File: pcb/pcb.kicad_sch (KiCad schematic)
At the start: 65 parts, among them J1 RJ45, J2 RJ45, SW1 Keyswitch, SW10 Keyswitch, SW11 Keyswitch, SW12 Keyswitch, SW13 Keyswitch, SW14 Keyswitch, SW15 Keyswitch, SW16 Keyswitch, SW17 Keyswitch, SW18 Keyswitch, SW19 Keyswitch, SW2 Keyswitch, SW20 Keyswitch, SW21 Keyswitch, SW22 Keyswitch, SW23 Keyswitch, SW24 Keyswitch, SW25 Keyswitch, SW26 Keyswitch, SW27 Keyswitch, SW28 Keyswitch, SW29 Keyswitch, SW3 Keyswitch, SW30 Keyswitch, SW4 Keyswitch, SW5 Keyswitch, SW6 Keyswitch, SW7 Keyswitch, SW8 Keyswitch, SW9 Keyswitch

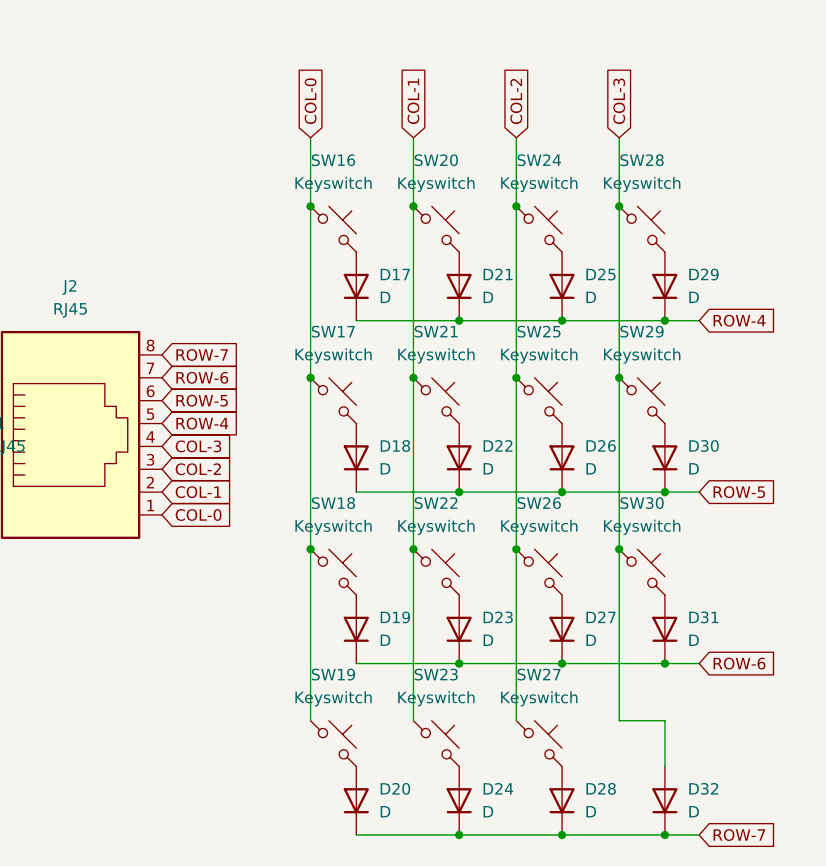
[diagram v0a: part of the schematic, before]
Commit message: add pcb right hand layout
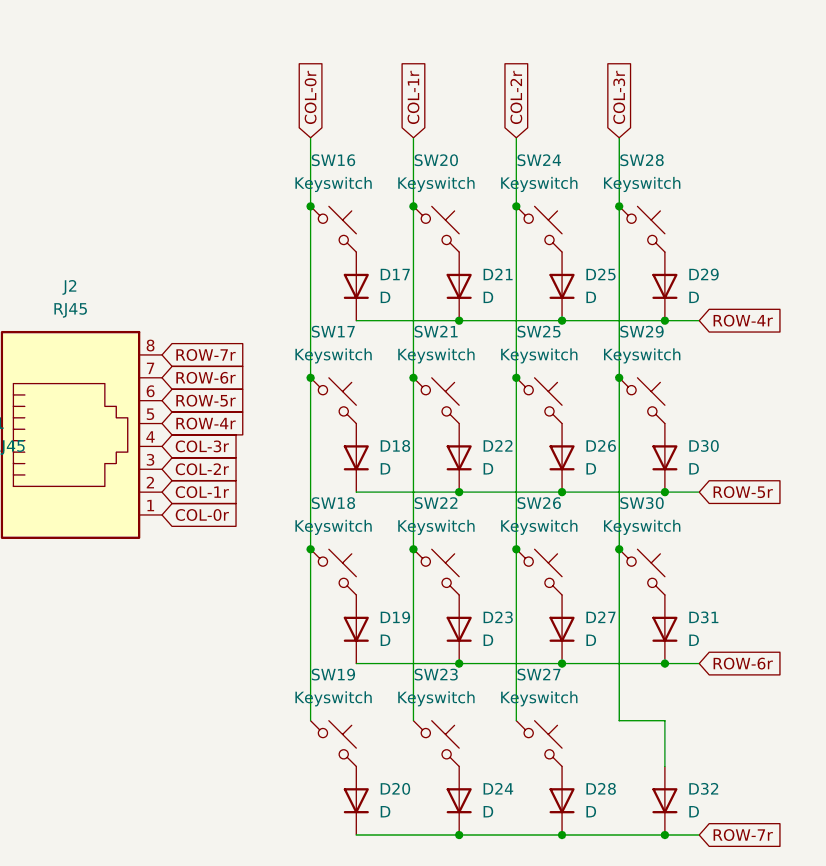
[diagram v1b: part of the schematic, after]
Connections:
- net COL-0: no longer J2.1, SW16.1, SW17.1, SW18.1, SW19.1
- net COL-1: no longer J2.2, SW20.1, SW21.1, SW22.1, SW23.1
- net COL-2: no longer J2.3, SW24.1, SW25.1, SW26.1, SW27.1
- net COL-3: no longer D32.2 (A), J2.4, SW28.1, SW29.1, SW30.1
- net ROW-4: no longer D17.1 (K), D21.1 (K), D25.1 (K), D29.1 (K), J2.5
- net ROW-5: no longer D18.1 (K), D22.1 (K), D26.1 (K), D30.1 (K), J2.6
- net ROW-6: no longer D19.1 (K), D23.1 (K), D27.1 (K), D31.1 (K), J2.7
- net ROW-7: no longer D20.1 (K), D24.1 (K), D28.1 (K), D32.1 (K), J2.8
- new net COL-0r: J2.1, SW16.1, SW17.1, SW18.1, SW19.1
- new net COL-1r: J2.2, SW20.1, SW21.1, SW22.1, SW23.1
- new net COL-2r: J2.3, SW24.1, SW25.1, SW26.1, SW27.1
- new net COL-3r: D32.2 (A), J2.4, SW28.1, SW29.1, SW30.1
- new net ROW-4r: D17.1 (K), D21.1 (K), D25.1 (K), D29.1 (K), J2.5
- new net ROW-5r: D18.1 (K), D22.1 (K), D26.1 (K), D30.1 (K), J2.6
- new net ROW-6r: D19.1 (K), D23.1 (K), D27.1 (K), D31.1 (K), J2.7
- new net ROW-7r: D20.1 (K), D24.1 (K), D28.1 (K), D32.1 (K), J2.8

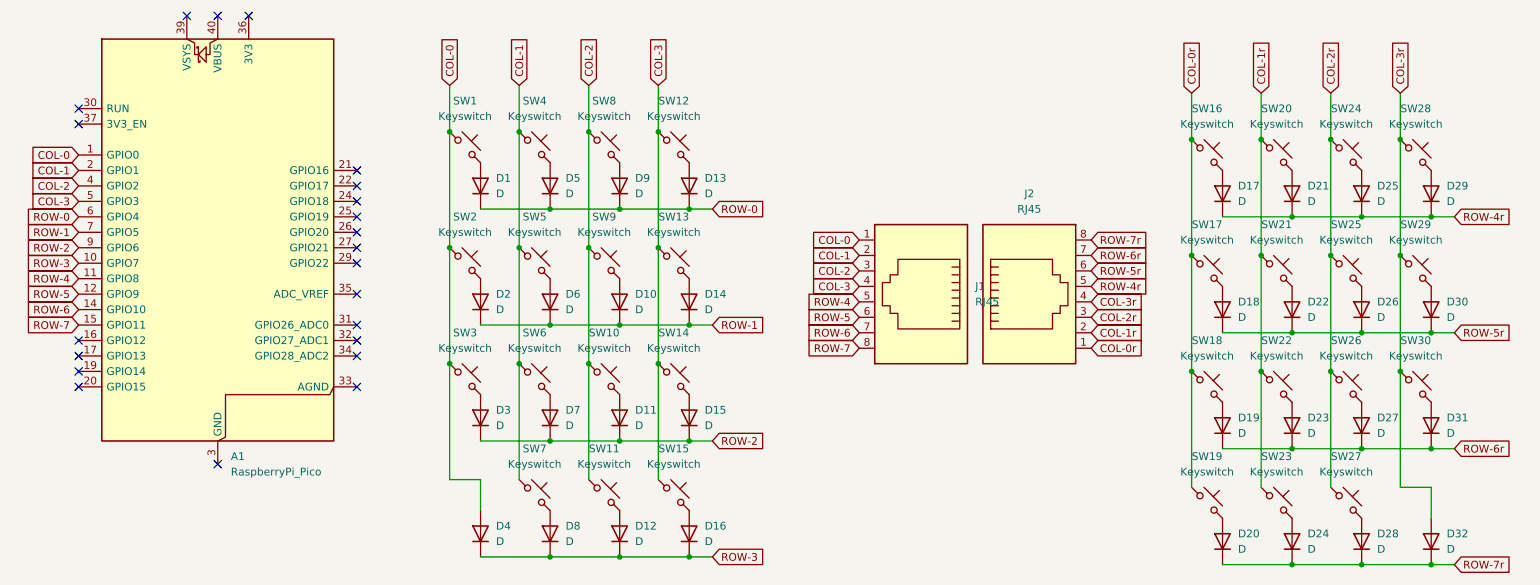
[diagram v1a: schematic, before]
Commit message: add pcb screw holes
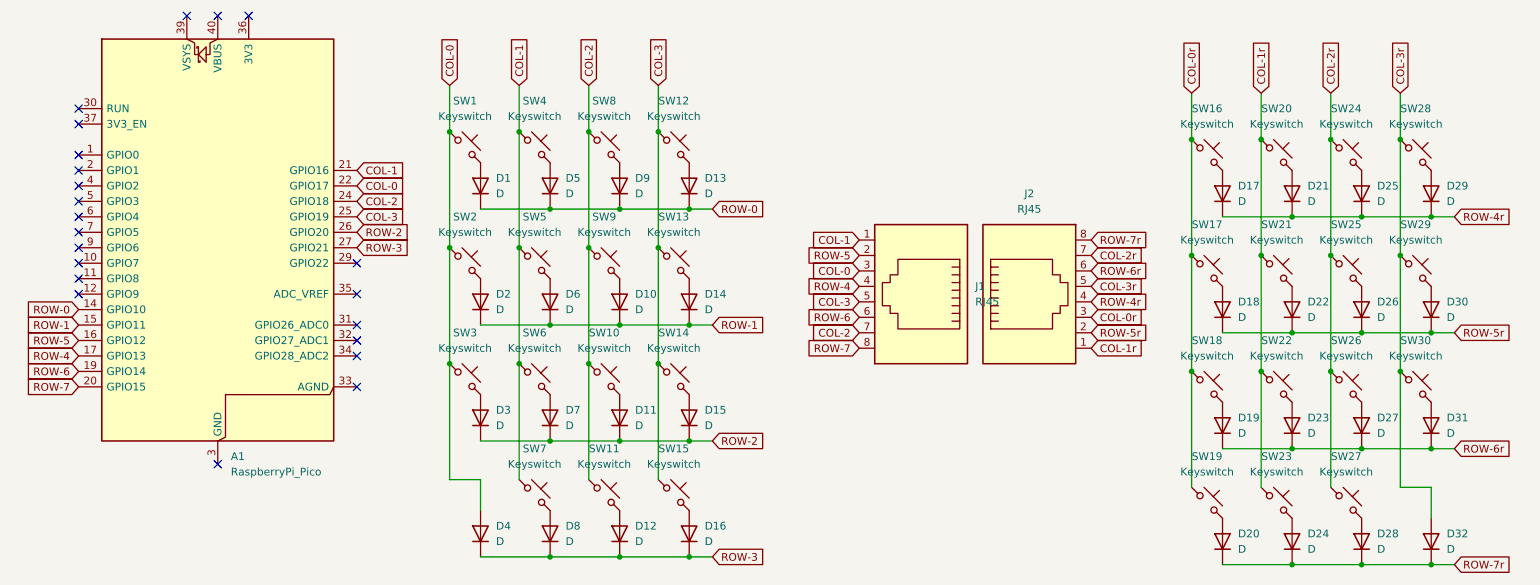
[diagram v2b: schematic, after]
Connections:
- net COL-0: now also A1.22 (GPIO17), J1.3; no longer A1.1 (GPIO0), J1.1
- net COL-0r: now also J2.3; no longer J2.1
- net COL-1: now also A1.21 (GPIO16), J1.1; no longer A1.2 (GPIO1), J1.2
- net COL-1r: now also J2.1; no longer J2.2
- net COL-2: now also A1.24 (GPIO18), J1.7; no longer A1.4 (GPIO2), J1.3
- net COL-2r: now also J2.7; no longer J2.3
- net COL-3: now also A1.25 (GPIO19), J1.5; no longer A1.5 (GPIO3), J1.4
- net COL-3r: now also J2.5; no longer J2.4
- net ROW-0: now also A1.14 (GPIO10); no longer A1.6 (GPIO4)
- net ROW-1: now also A1.15 (GPIO11); no longer A1.7 (GPIO5)
- net ROW-2: now also A1.26 (GPIO20); no longer A1.9 (GPIO6)
- net ROW-3: now also A1.27 (GPIO21); no longer A1.10 (GPIO7)
- net ROW-4: now also A1.17 (GPIO13), J1.4; no longer A1.11 (GPIO8), J1.5
- net ROW-4r: now also J2.4; no longer J2.5
- net ROW-5: now also A1.16 (GPIO12), J1.2; no longer A1.12 (GPIO9), J1.6
- net ROW-5r: now also J2.2; no longer J2.6
- net ROW-6: now also A1.19 (GPIO14), J1.6; no longer A1.14 (GPIO10), J1.7
- net ROW-6r: now also J2.6; no longer J2.7
- net ROW-7: now also A1.20 (GPIO15); no longer A1.15 (GPIO11)

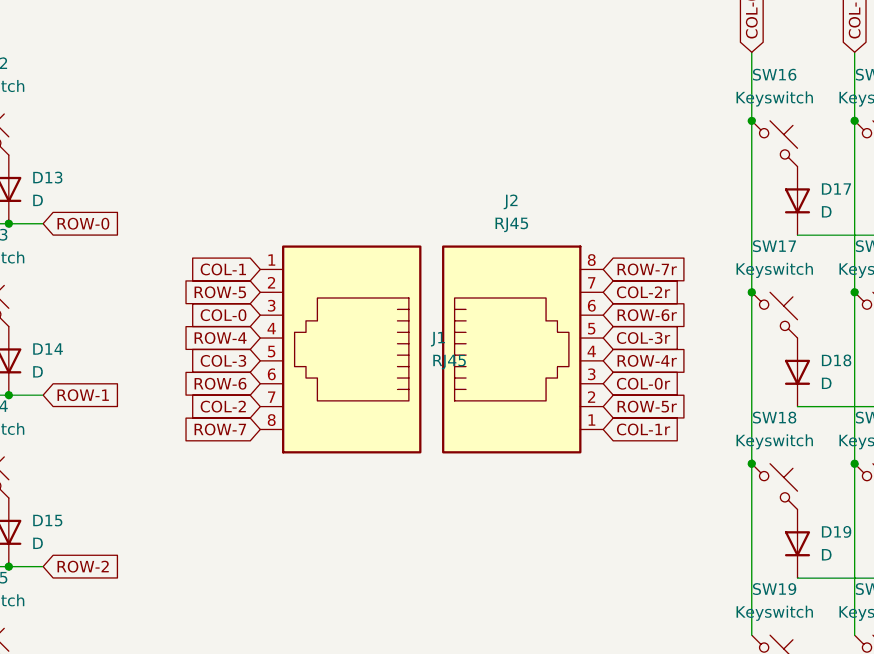
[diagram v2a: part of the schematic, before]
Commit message: fix pcb holes
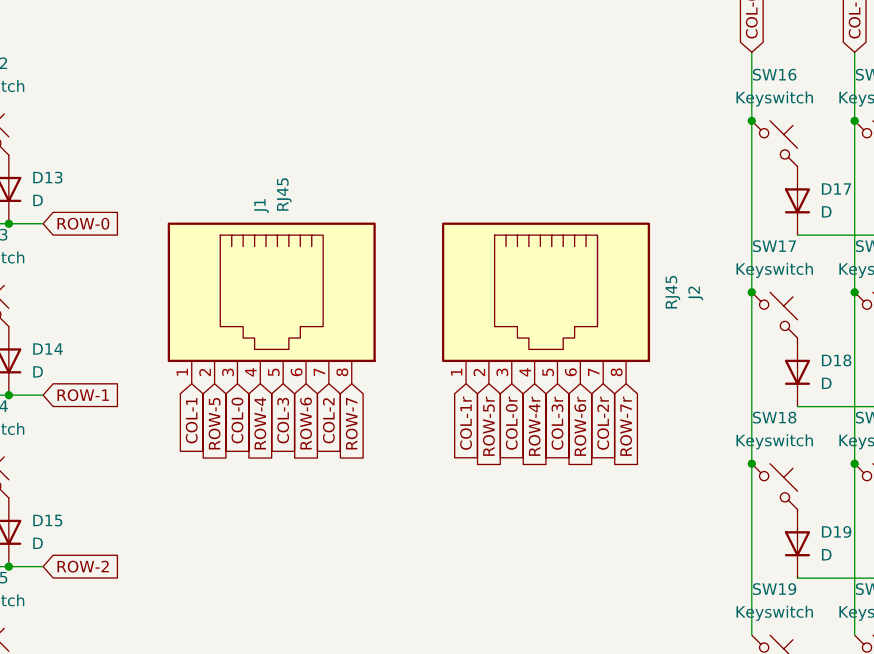
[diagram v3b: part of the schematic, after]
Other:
- moved on the sheet: J1, J2
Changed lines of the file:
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@@
 	(global_label "COL-1r"
 		(shape input)
-		(at 194.31 73.66 0)
+		(at 179.07 68.58 270)
 		(fields_autoplaced yes)
 		(effects
@@
 				(size 1.27 1.27)
 			)
-			(justify left)
+			(justify right)
 		)
 		(property "Intersheetrefs" "${INTERSHEET_REFS}"
-			(at 204.4919 73.66 0)
+			(at 179.07 78.7619 90)
 			(effects
 				(font
 					(size 1.27 1.27)
 				)
-				(justify left)
+				(justify right)
 				(hide yes)
 			)
@@
 	(global_label "ROW-6r"
 		(shape input)
-		(at 194.31 60.96 0)
+		(at 191.77 68.58 270)
 		(fields_autoplaced yes)
 		(effects
@@
 				(size 1.27 1.27)
 			)
-			(justify left)
+			(justify right)
 		)
 		(property "Intersheetrefs" "${INTERSHEET_REFS}"
-			(at 204.9152 60.96 0)
+			(at 191.77 79.1852 90)
 			(effects
 				(font
 					(size 1.27 1.27)
 				)
-				(justify left)
+				(justify right)
 				(hide yes)
 			)
@@
 	(global_label "ROW-5"
 		(shape input)
-		(at 156.21 58.42 180)
+		(at 151.13 68.58 270)
 		(fields_autoplaced yes)
 		(effects
@@
 		)
 		(property "Intersheetrefs" "${INTERSHEET_REFS}"
-			(at 146.391 58.42 0)
+			(at 151.13 78.399 90)
 			(effects
 				(font
@@
 	(global_label "ROW-4"
 		(shape input)
-		(at 156.21 63.5 180)
+		(at 156.21 68.58 270)
 		(fields_autoplaced yes)
 		(effects
@@
 		)
 		(property "Intersheetrefs" "${INTERSHEET_REFS}"
-			(at 146.391 63.5 0)
+			(at 156.21 78.399 90)
 			(effects
 				(font
@@
 	(global_label "ROW-4r"
 		(shape input)
-		(at 194.31 66.04 0)
+		(at 186.69 68.58 270)
 		(fields_autoplaced yes)
 		(effects
@@
 				(size 1.27 1.27)
 			)
-			(justify left)
+			(justify right)
 		)
 		(property "Intersheetrefs" "${INTERSHEET_REFS}"
-			(at 204.9152 66.04 0)
+			(at 186.69 79.1852 90)
 			(effects
 				(font
 					(size 1.27 1.27)
 				)
-				(justify left)
+				(justify right)
 				(hide yes)
 			)
@@
 	(global_label "ROW-7"
 		(shape input)
-		(at 156.21 73.66 180)
+		(at 166.37 68.58 270)
 		(fields_autoplaced yes)
 		(effects
@@
 		)
 		(property "Intersheetrefs" "${INTERSHEET_REFS}"
-			(at 146.391 73.66 0)
+			(at 166.37 78.399 90)
 			(effects
 				(font
@@
 	(global_label "COL-2"
 		(shape input)
-		(at 156.21 71.12 180)
+		(at 163.83 68.58 270)
 		(fields_autoplaced yes)
 		(effects
@@
 		)
 		(property "Intersheetrefs" "${INTERSHEET_REFS}"
-			(at 146.8143 71.12 0)
+			(at 163.83 77.9757 90)
 			(effects
 				(font
@@
 	(global_label "ROW-5r"
 		(shape input)
-		(at 194.31 71.12 0)
+		(at 181.61 68.58 270)
 		(fields_autoplaced yes)
 		(effects
@@
 				(size 1.27 1.27)
 			)
-			(justify left)
+			(justify right)
 		)
 		(property "Intersheetrefs" "${INTERSHEET_REFS}"
-			(at 204.9152 71.12 0)
+			(at 181.61 79.1852 90)
 			(effects
 				(font
 					(size 1.27 1.27)
 				)
-				(justify left)
+				(justify right)
 				(hide yes)
 			)
@@
 	(global_label "ROW-6"
 		(shape input)
-		(at 156.21 68.58 180)
+		(at 161.29 68.58 270)
 		(fields_autoplaced yes)
 		(effects
@@
 		)
 		(property "Intersheetrefs" "${INTERSHEET_REFS}"
-			(at 146.391 68.58 0)
+			(at 161.29 78.399 90)
 			(effects
 				(font
@@
 	(global_label "ROW-7r"
 		(shape input)
-		(at 194.31 55.88 0)
+		(at 196.85 68.58 270)
 		(fields_autoplaced yes)
 		(effects
@@
 				(size 1.27 1.27)
 			)
-			(justify left)
+			(justify right)
 		)
 		(property "Intersheetrefs" "${INTERSHEET_REFS}"
-			(at 204.9152 55.88 0)
+			(at 196.85 79.1852 90)
 			(effects
 				(font
 					(size 1.27 1.27)
 				)
-				(justify left)
+				(justify right)
 				(hide yes)
 			)
@@
 	(global_label "COL-3r"
 		(shape input)
-		(at 194.31 63.5 0)
+		(at 189.23 68.58 270)
 		(fields_autoplaced yes)
 		(effects
@@
 				(size 1.27 1.27)
 			)
-			(justify left)
+			(justify right)
 		)
 		(property "Intersheetrefs" "${INTERSHEET_REFS}"
-			(at 204.4919 63.5 0)
+			(at 189.23 78.7619 90)
 			(effects
 				(font
 					(size 1.27 1.27)
 				)
-				(justify left)
+				(justify right)
 				(hide yes)
 			)
@@
 	(global_label "COL-0r"
 		(shape input)
-		(at 194.31 68.58 0)
+		(at 184.15 68.58 270)
 		(fields_autoplaced yes)
 		(effects
@@
 				(size 1.27 1.27)
 			)
-			(justify left)
+			(justify right)
 		)
 		(property "Intersheetrefs" "${INTERSHEET_REFS}"
-			(at 204.4919 68.58 0)
+			(at 184.15 78.7619 90)
 			(effects
 				(font
 					(size 1.27 1.27)
 				)
-				(justify left)
+				(justify right)
 				(hide yes)
 			)
@@
 	(global_label "COL-2r"
 		(shape input)
-		(at 194.31 58.42 0)
+		(at 194.31 68.58 270)
 		(fields_autoplaced yes)
 		(effects
@@
 				(size 1.27 1.27)
 			)
-			(justify left)
+			(justify right)
 		)
 		(property "Intersheetrefs" "${INTERSHEET_REFS}"
-			(at 204.4919 58.42 0)
+			(at 194.31 78.7619 90)
 			(effects
 				(font
 					(size 1.27 1.27)
 				)
-				(justify left)
+				(justify right)
 				(hide yes)
 			)
@@
 	(global_label "COL-3"
 		(shape input)
-		(at 156.21 66.04 180)
+		(at 158.75 68.58 270)
 		(fields_autoplaced yes)
 		(effects
@@
 		)
 		(property "Intersheetrefs" "${INTERSHEET_REFS}"
-			(at 146.8143 66.04 0)
+			(at 158.75 77.9757 90)
 			(effects
 				(font
@@
 	(global_label "COL-0"
 		(shape input)
-		(at 156.21 60.96 180)
+		(at 153.67 68.58 270)
 		(fields_autoplaced yes)
 		(effects
@@
 		)
 		(property "Intersheetrefs" "${INTERSHEET_REFS}"
-			(at 146.8143 60.96 0)
+			(at 153.67 77.9757 90)
 			(effects
 				(font
@@
 	(global_label "COL-1"
 		(shape input)
-		(at 156.21 55.88 180)
+		(at 148.59 68.58 270)
 		(fields_autoplaced yes)
 		(effects
@@
 		)
 		(property "Intersheetrefs" "${INTERSHEET_REFS}"
-			(at 146.8143 55.88 0)
+			(at 148.59 77.9757 90)
 			(effects
 				(font
@@
 	(symbol
 		(lib_id "Connector:RJ45")
-		(at 184.15 66.04 0)
+		(at 186.69 58.42 270)
 		(unit 1)
 		(exclude_from_sim no)
@@
 		(fields_autoplaced yes)
 		(property "Reference" "J2"
-			(at 184.15 48.26 0)
+			(at 204.47 58.42 0)
 			(effects
 				(font
@@
 		)
 		(property "Value" "RJ45"
-			(at 184.15 50.8 0)
+			(at 201.93 58.42 0)
 			(effects
 				(font
@@
 		)
 		(property "Footprint" "Connector_RJ:RJ45_Amphenol_54602-x08_Horizontal"
-			(at 184.15 65.405 90)
+			(at 187.325 58.42 90)
 			(effects
 				(font
@@
 		)
 		(property "Datasheet" "~"
-			(at 184.15 65.405 90)
+			(at 187.325 58.42 90)
 			(effects
 				(font
@@
 		)
 		(property "Description" "RJ connector, 8P8C (8 positions 8 connected)"
-			(at 184.15 66.04 0)
+			(at 186.69 58.42 0)
 			(effects
 				(font
@@
 	(symbol
 		(lib_id "Connector:RJ45")
-		(at 166.37 63.5 180)
+		(at 156.21 58.42 270)
 		(unit 1)
 		(exclude_from_sim no)
@@
 		(fields_autoplaced yes)
 		(property "Reference" "J1"
-			(at 175.26 63.4999 0)
+			(at 156.2099 49.53 0)
 			(effects
 				(font
@@
 		)
 		(property "Value" "RJ45"
-			(at 175.26 66.0399 0)
+			(at 158.7499 49.53 0)
 			(effects
 				(font
@@
 		)
 		(property "Footprint" "Connector_RJ:RJ45_Amphenol_54602-x08_Horizontal"
-			(at 166.37 64.135 90)
+			(at 156.845 58.42 90)
 			(effects
 				(font
@@
 		)
 		(property "Datasheet" "~"
-			(at 166.37 64.135 90)
+			(at 156.845 58.42 90)
 			(effects
 				(font
@@
 		)
 		(property "Description" "RJ connector, 8P8C (8 positions 8 connected)"
-			(at 166.37 63.5 0)
+			(at 156.21 58.42 0)
 			(effects
 				(font
